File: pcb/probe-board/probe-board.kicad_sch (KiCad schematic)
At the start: 27 parts, among them J1 Conn_ARM_SWD_TagConnect_TC203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, J2 USB_C_Receptacle_USB2.0_16P, U1 STM32G431KBUx, U2 SRV05-4, U3 AMS1117-3.3, Y1 16MHz

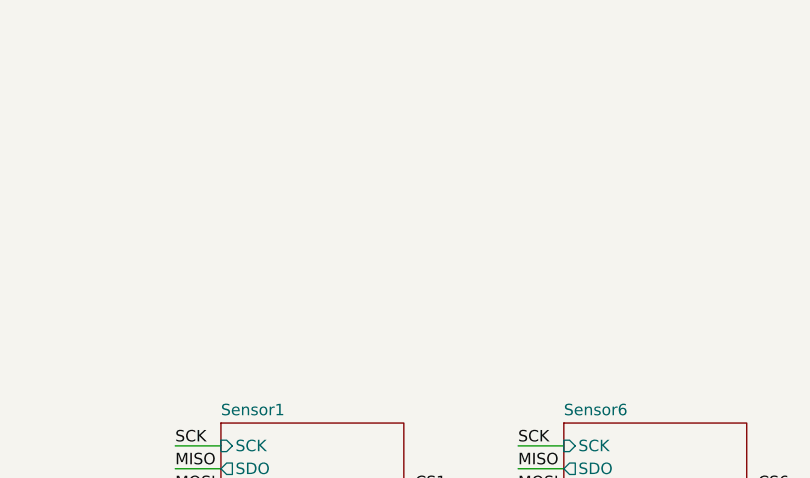
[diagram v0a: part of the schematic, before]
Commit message: Add feducials
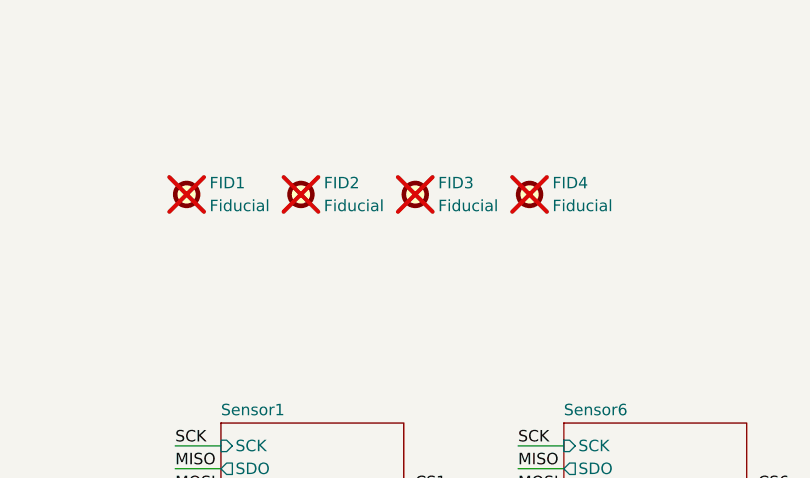
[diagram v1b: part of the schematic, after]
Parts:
- added FID1, FID2, FID3, FID4: Fiducial, Fiducial:Fiducial_1mm_Mask2mm, symbol Mechanical:Fiducial

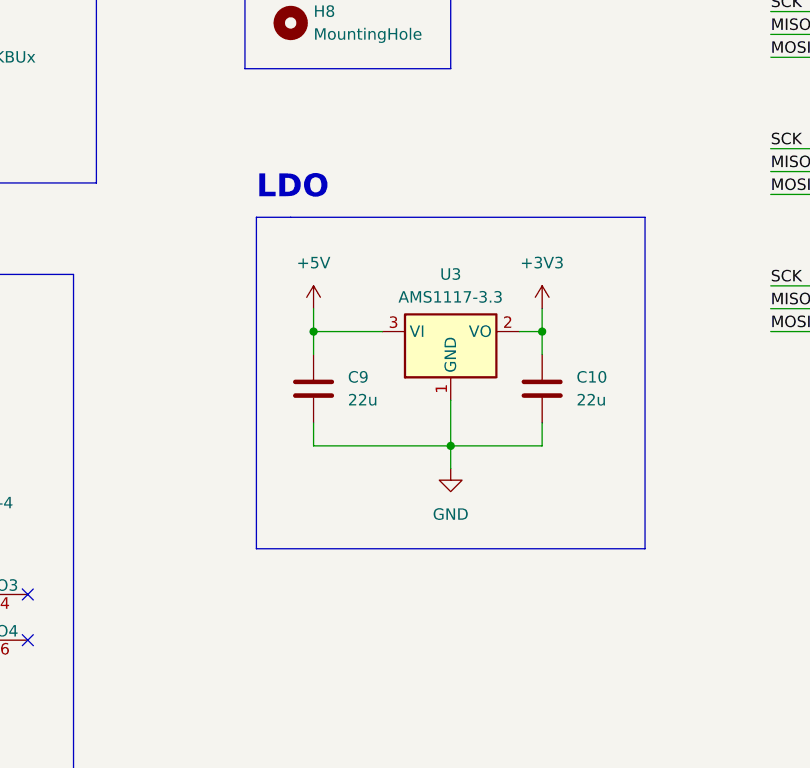
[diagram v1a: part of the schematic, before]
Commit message: Add feducials and new manufacture data
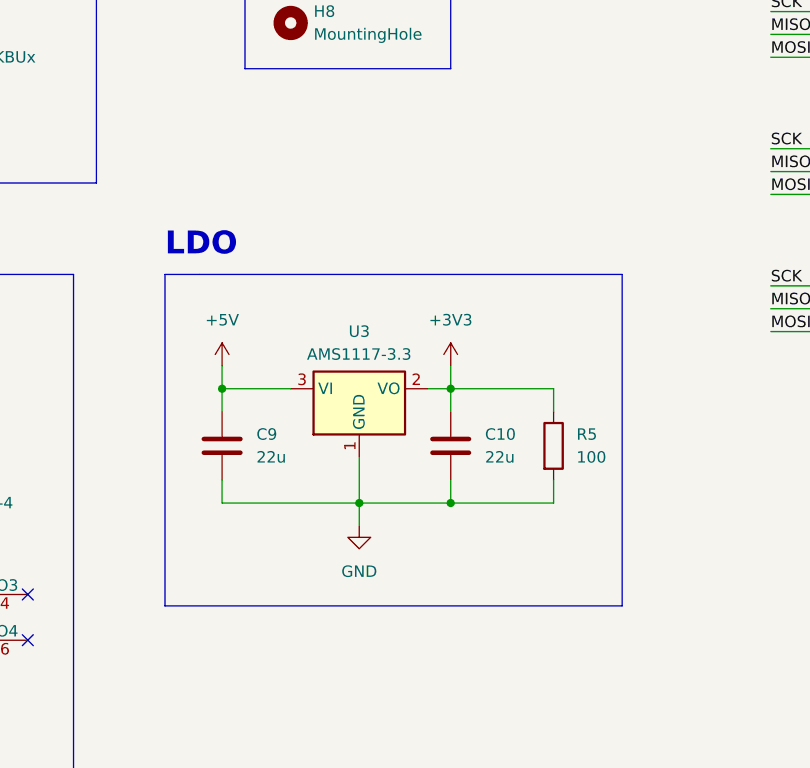
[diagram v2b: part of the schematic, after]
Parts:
- added R5: 100, Resistor_SMD:R_0805_2012Metric, symbol Device:R
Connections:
- net +3V3: now also R5.1
- net GND: now also R5.2
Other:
- moved on the sheet: C10, C9, U3
